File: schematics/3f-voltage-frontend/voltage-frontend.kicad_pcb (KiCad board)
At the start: 2 copper layers, 100 x 44 mm, 16 parts, among them P1 L3 L2 L1 N, P2 6V AC OUT L1, P3 6V AC OUT L3, P4 6V AC OUT L2, P5 mounting hole, P6 mounting hole, P7 mounting hole, P8 mounting hole, T1 TRANSFO, T2 TRANSFO, T3 TRANSFO

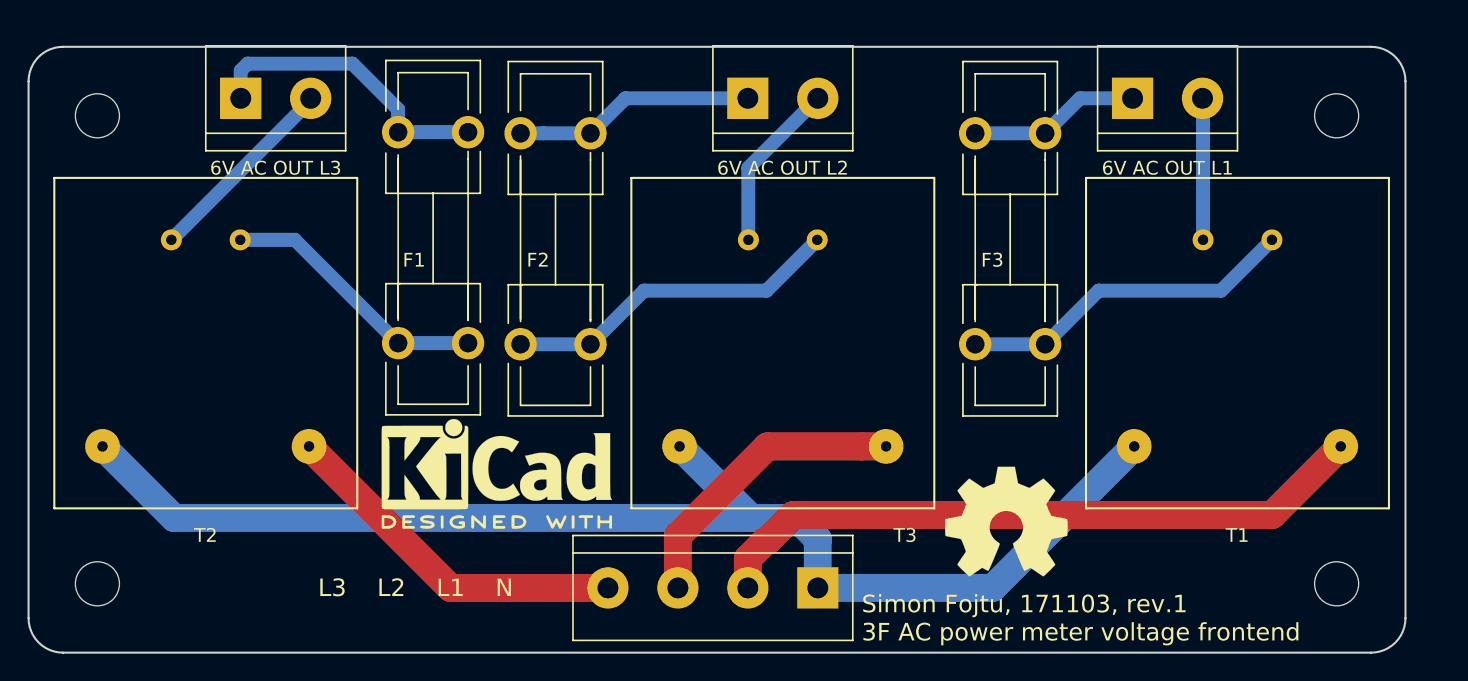
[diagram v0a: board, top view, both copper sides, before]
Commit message: 3F frontend - shrunk pcb
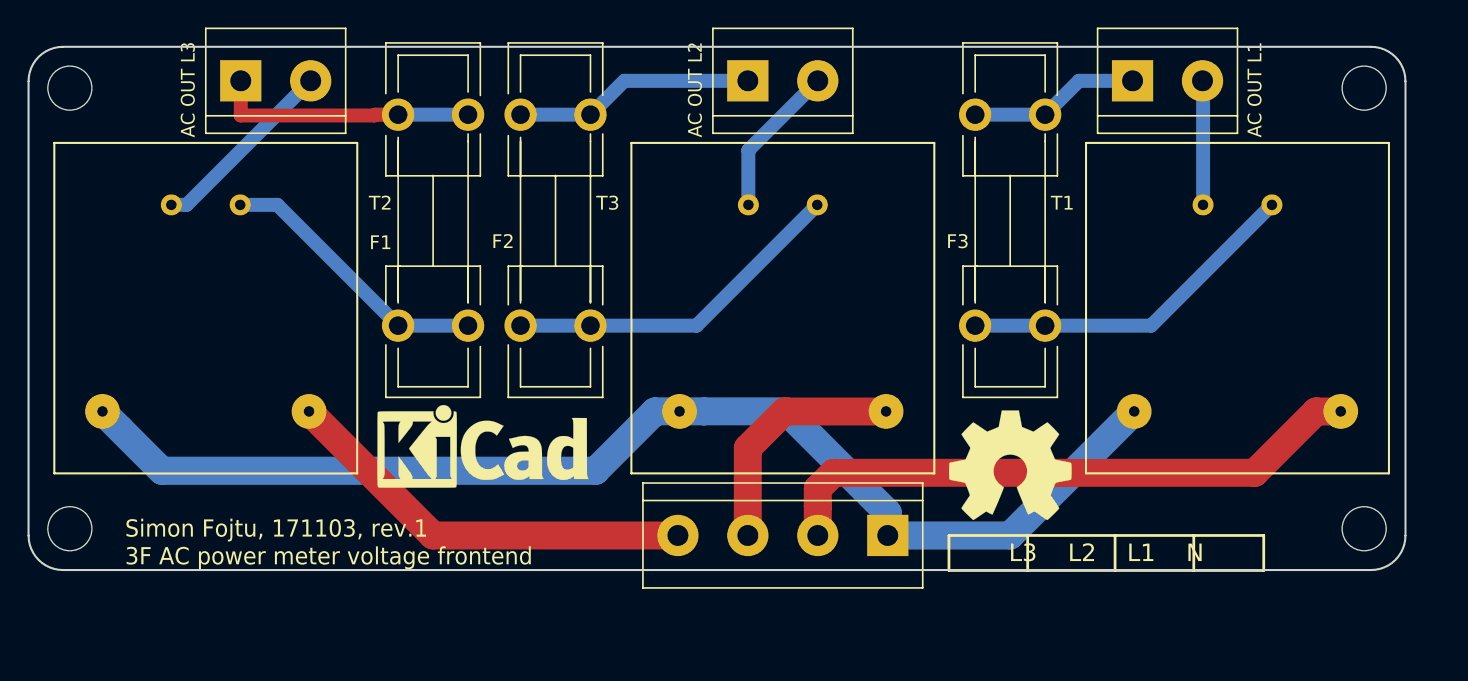
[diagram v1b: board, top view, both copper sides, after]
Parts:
- removed the REF*** at (124.0, 106.0)
- added REF***: KiCad-Logo_6mm_SilkScreen, Symbols:KiCad-Logo_6mm_SilkScreen, F.Cu at (123.0, 104.0)
- P2: value 6V AC OUT L1 -> AC OUT L1
- P3: value 6V AC OUT L3 -> AC OUT L3
- P4: value 6V AC OUT L2 -> AC OUT L2
- moved P1 6.35 mm to (152.4, 110.5)
- moved P6 4.47 mm to (187.0, 110.0)
- moved P7 4.47 mm to (93.0, 110.0)
- moved REF*** 4.10 mm to (161.3, 105.4)
- moved P5 2.84 mm to (187.0, 78.0)
- moved P8 2.84 mm to (93.0, 78.0)
- moved T1 2.54 mm to (177.8, 94.0)
- moved T2 2.54 mm to (102.9, 94.0)
- moved T3 2.54 mm to (144.8, 94.0)
- moved F2 1.35 mm to (125.7, 95.2)
- moved F3 1.35 mm to (158.8, 95.2)
- moved F1 1.27 mm to (116.8, 95.2)
- moved P2 1.27 mm to (170.2, 77.5)
- moved P3 1.27 mm to (105.4, 77.5)
- moved P4 1.27 mm to (142.2, 77.5)
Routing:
- net GND: track 92.9 -> 86.9 mm
- net Net-(P1-Pad2): track 48.6 -> 43.7 mm
- net Net-(P1-Pad4): track 26.0 -> 30.5 mm
- net Net-(P1-Pad3): track 21.6 -> 17.5 mm
- net Net-(F1-Pad2): track 21.8 -> 19.0 mm
- net Net-(P4-Pad2): track 12.4 -> 11.1 mm
- net Net-(P2-Pad2): track 10.3 -> 9.03 mm
- net Net-(P3-Pad2): track 14.5 -> 13.9 mm
- net Net-(F1-Pad1): track 19.7 -> 20.2 mm
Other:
- board size 100 x 44 mm -> 100 x 38 mm
